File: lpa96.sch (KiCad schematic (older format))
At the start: 26 parts, among them IC1 ATMEGA328-A, P1 CONN_2, P2 CONN_3X2, SW1 SW_PUSH, U1 SD_CARD, U2 LD1117S33, Y1 RESONATEUR

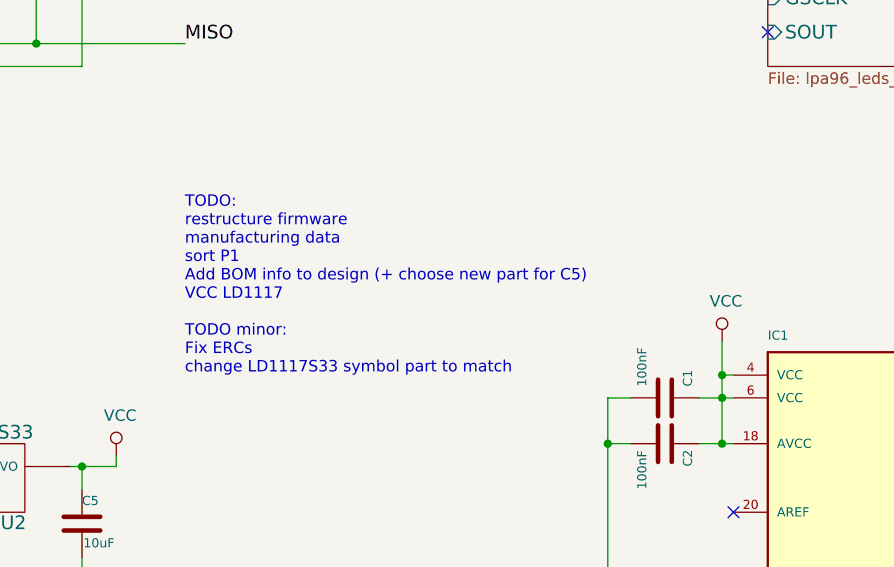
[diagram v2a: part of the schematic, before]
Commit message: done titleblocks, added silkscreen logos
added OSHW and ESD logos to board
filled in titleblocks with title, revision, date, authors
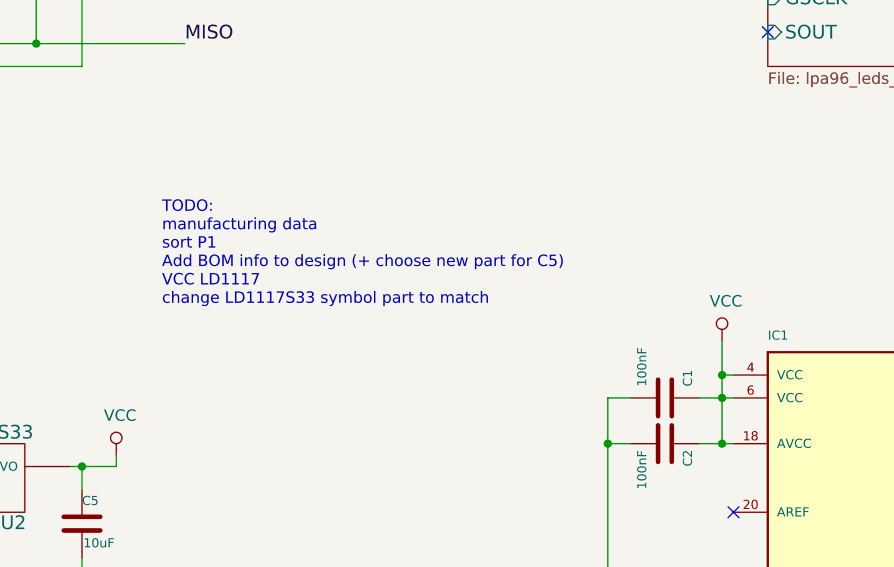
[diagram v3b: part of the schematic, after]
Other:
- note added: "TODO:\nmanufacturing data\nsort P1\nAdd BOM info to design (+ choose new part for C5)\nVCC LD1117\nchange LD1117S33 symbol part to match"
- note removed: "TODO:\nrestructure firmware\nmanufacturing data\nsort P1\nAdd BOM info to design (+ choose new part for C5)\nVCC LD1117\n\nTODO minor:\nFix ERCs\nchange LD1117S33 symbol part to match"
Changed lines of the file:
@@
 encoding utf-8
 Sheet 1 2
-Title ""
-Date "25 jun 2014"
-Rev ""
-Comp ""
+Title "96-well Light Plate Apparatus (LPA), Blue 465nm"
+Date "2019-08-22"
+Rev "2.0"
+Comp "Authors: Tabor lab/Evan Olson/Sebastian Castillo/Open Bioeconomy Lab/Kevin Bibby"
 Comment1 ""
 Comment2 ""
@@
 Text Notes 3650 5800 0    50   ~ 0
 SW1 - Switch to reset processor\nLED97 - lit when running\nLED98 - lit if error\nLED99 - lit once finished\n(LED behaviour software dependant)
-Text Notes 4400 3850 0    50   ~ 0
-TODO:\nrestructure firmware\nmanufacturing data\nsort P1\nAdd BOM info to design (+ choose new part for C5)\nVCC LD1117\n\nTODO minor:\nFix ERCs\nchange LD1117S33 symbol part to match
+Text Notes 4300 3550 0    50   ~ 0
+TODO:\nmanufacturing data\nsort P1\nAdd BOM info to design (+ choose new part for C5)\nVCC LD1117\nchange LD1117S33 symbol part to match
 Wire Wire Line
 	3950 4250 4100 4250

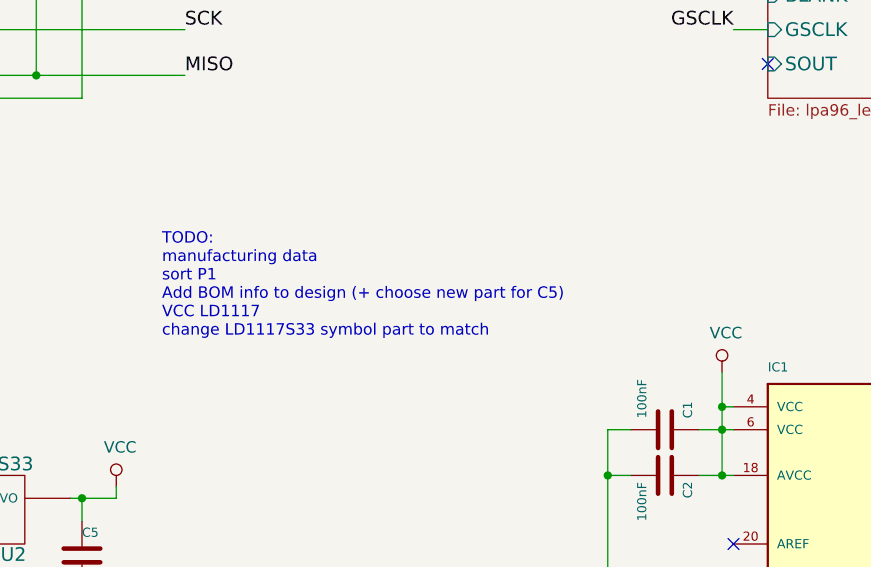
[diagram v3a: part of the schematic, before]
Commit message: title name change, exported final design pack
changed titleblock to remove "blue 465nm" to keep general, removed TODO text ready for export
added full export of design pack (schematic/layout pdfs, step model, gerbers, position & drill files)
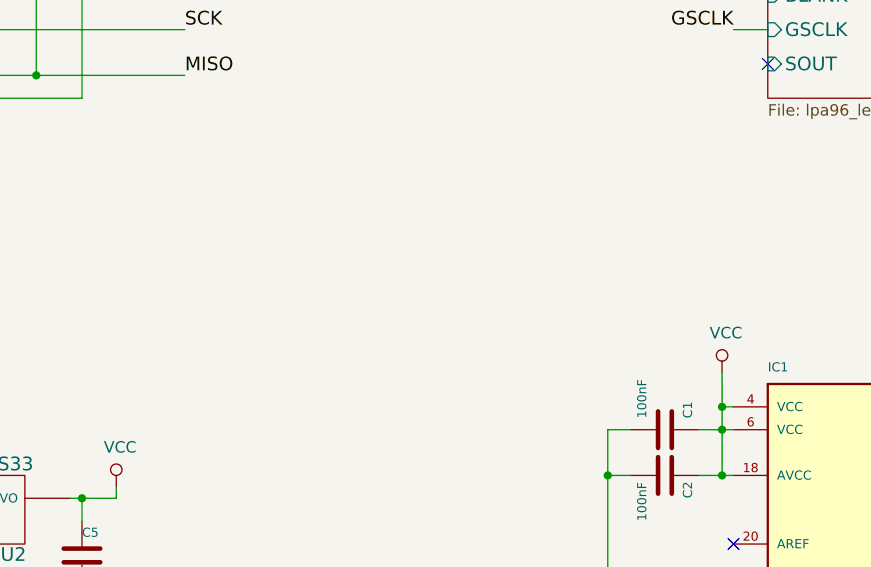
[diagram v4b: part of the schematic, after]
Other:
- note removed: "TODO:\nmanufacturing data\nsort P1\nAdd BOM info to design (+ choose new part for C5)\nVCC LD1117\nchange LD1117S33 symbol part to match"
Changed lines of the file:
@@
 encoding utf-8
 Sheet 1 2
-Title "96-well Light Plate Apparatus (LPA), Blue 465nm"
+Title "96-well Light Plate Apparatus (LPA)"
 Date "2019-08-22"
 Rev "2.0"
@@
 Text Notes 3650 5800 0    50   ~ 0
 SW1 - Switch to reset processor\nLED97 - lit when running\nLED98 - lit if error\nLED99 - lit once finished\n(LED behaviour software dependant)
-Text Notes 4300 3550 0    50   ~ 0
-TODO:\nmanufacturing data\nsort P1\nAdd BOM info to design (+ choose new part for C5)\nVCC LD1117\nchange LD1117S33 symbol part to match
 Wire Wire Line
 	3950 4250 4100 4250

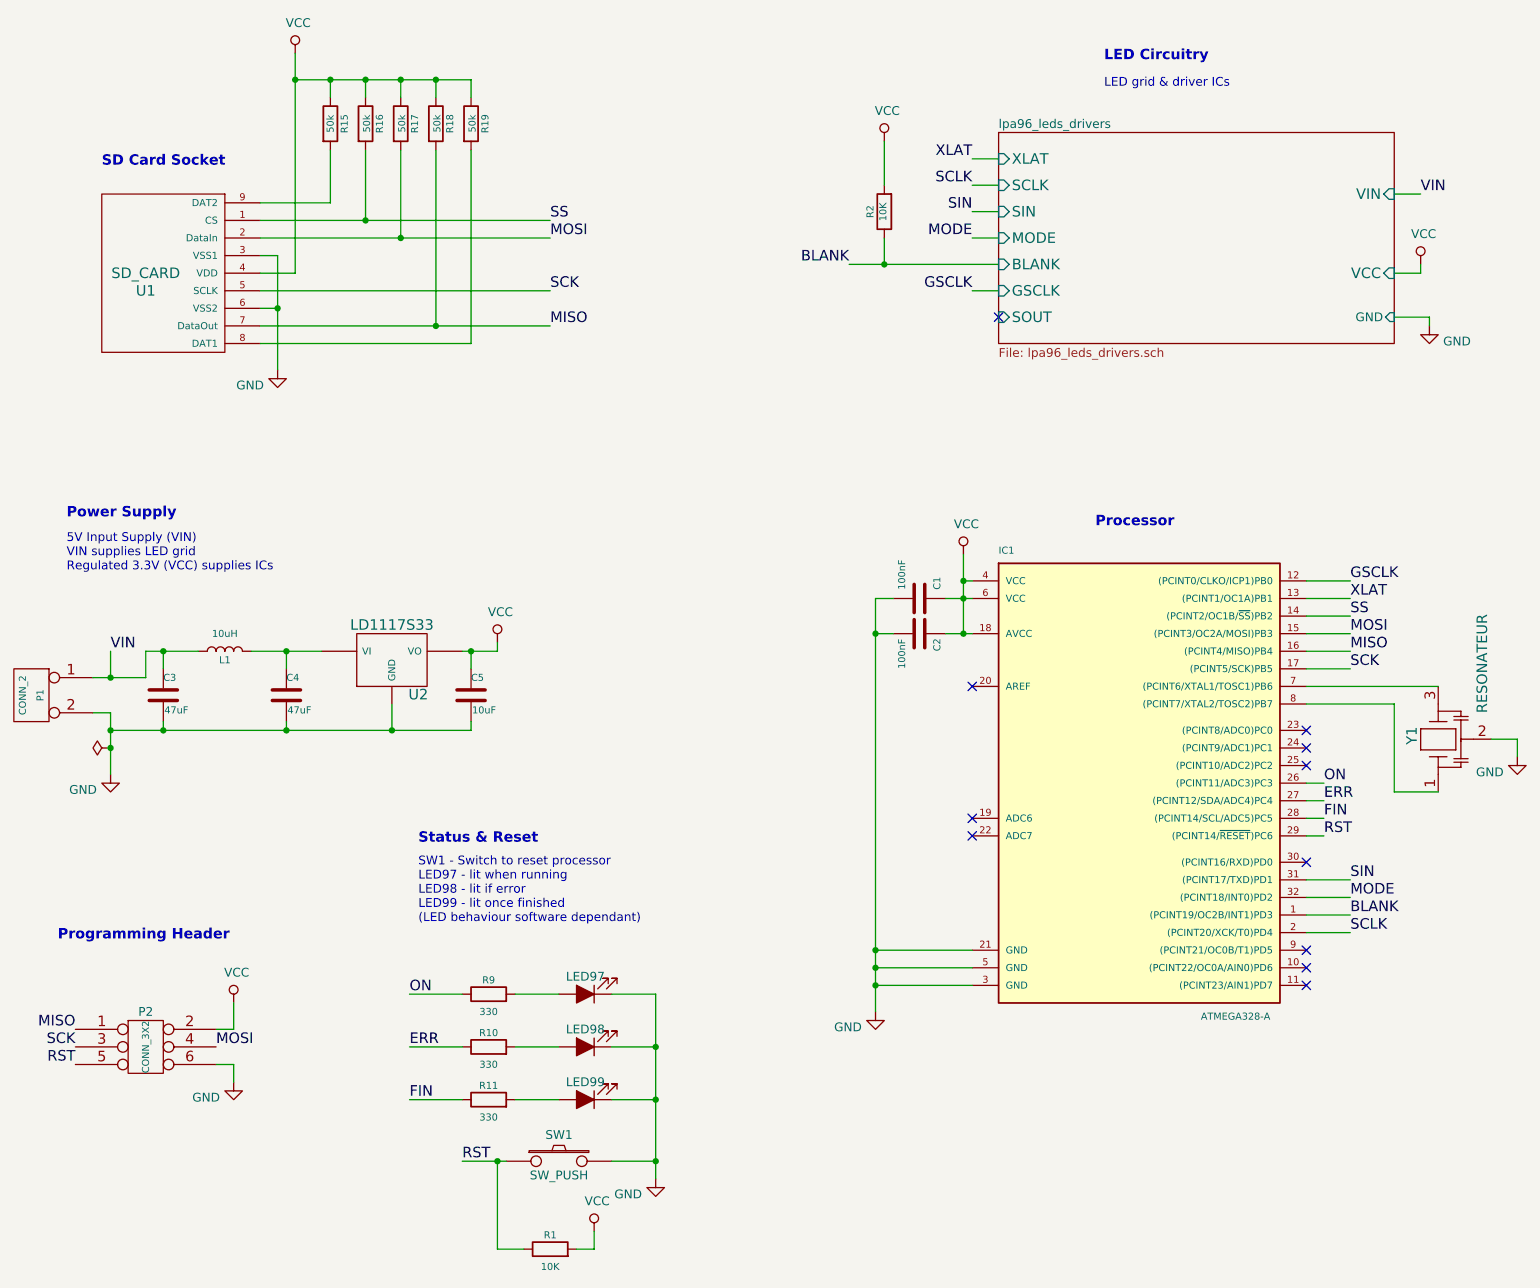
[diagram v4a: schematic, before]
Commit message: small tweaks, added component part numbers & descriptions into design
added all part info from original 24well LPA 'Nature' article (Supplementary Information, Table S1).
part info uses "Description", "Manufacturer1", "MPN1", "Vendor1" and "SKU1" part fields.
changed part info for new LED parts, and C5,C12 chosen part for new case size.
changed P2 to 2x3way exact part rather than 40way breakable header.
changed R15-R19 from 50k to 47k to match part number
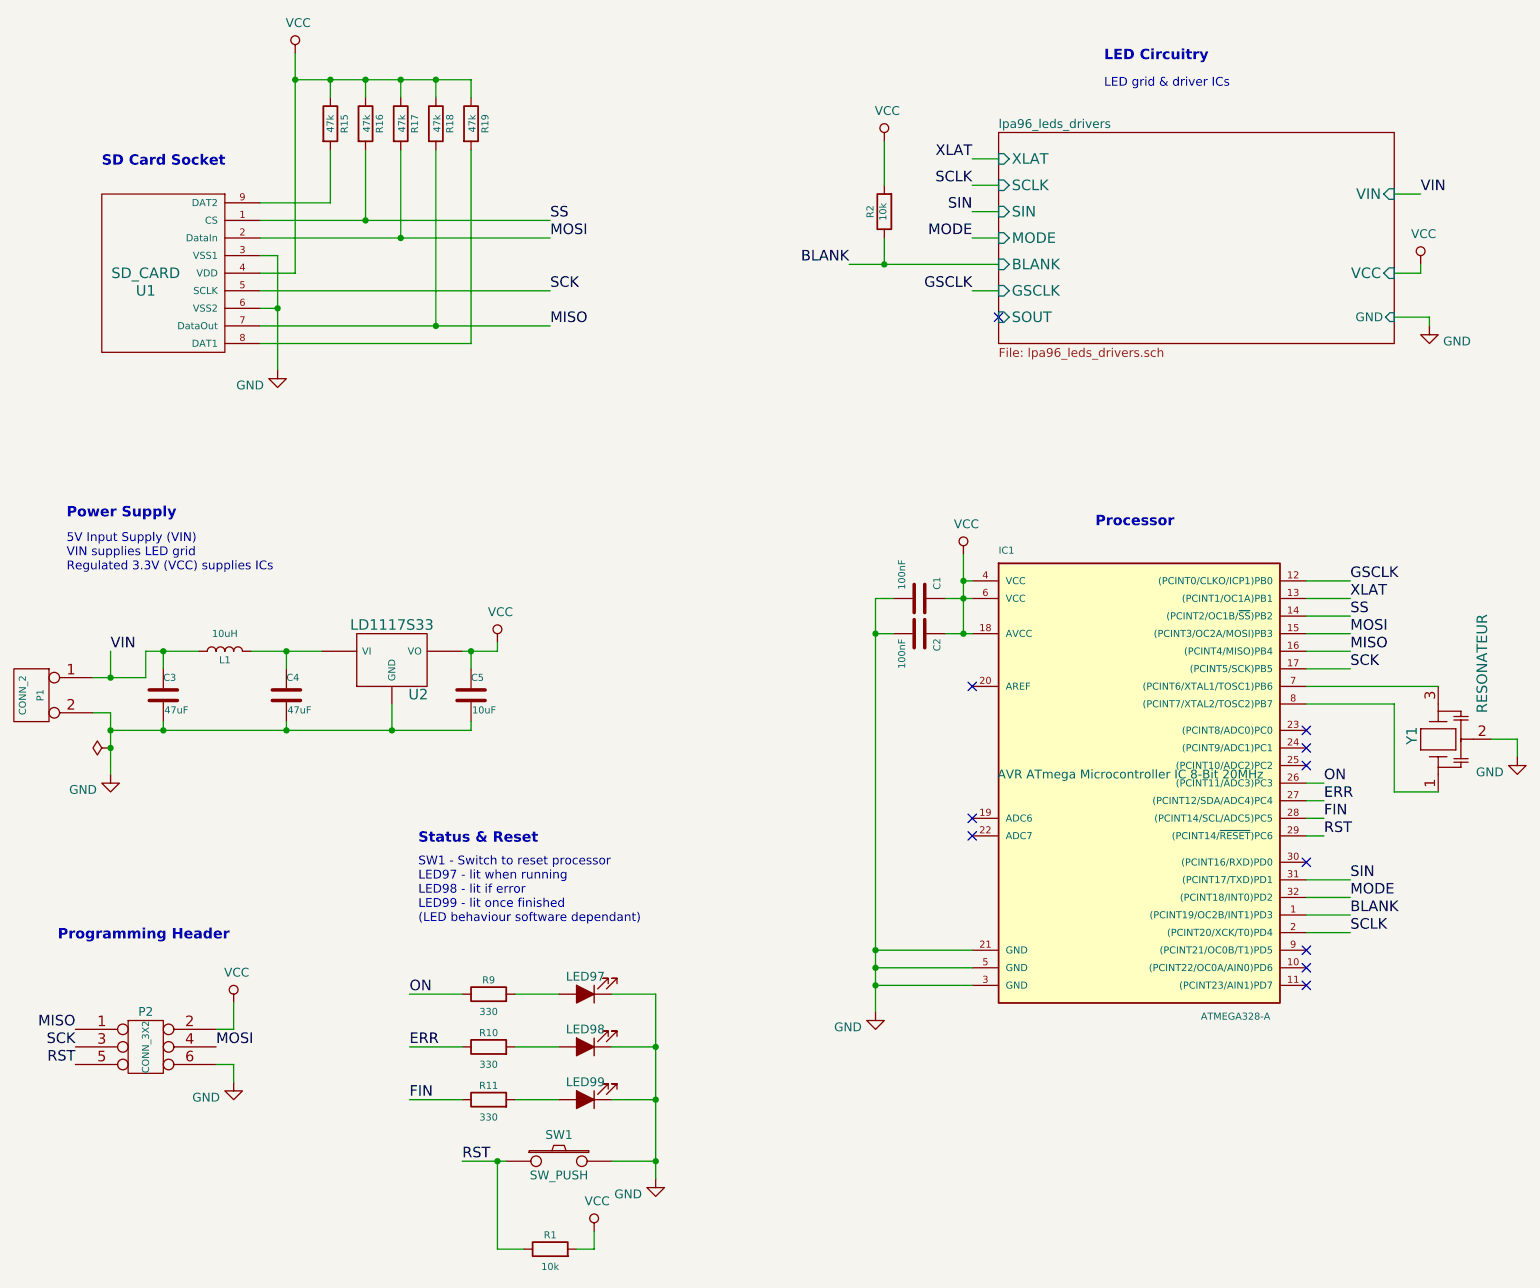
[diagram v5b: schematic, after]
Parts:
- C1, C2: Description (none) -> -20/+80% 50V Y5V SMD MLCC Capacitor 0805; MPN1 (none) -> CL21F104ZBCNNNC; Manufacturer1 (none) -> Samsung; SKU1 (none) -> 1276-1007-1-ND; Vendor1 (none) -> Digikey
- C3, C4: Description (none) -> 20% 35V SMD Electrolytic Capacitor; MPN1 (none) -> UWT1V470MCL1GS; Manufacturer1 (none) -> Nichicon; SKU1 (none) -> 493-2202-1-ND; Vendor1 (none) -> Digikey
- C5: Description (none) -> 10% 25V X5R SMD MLCC Capacitor 1206; MPN1 (none) -> CL31A106KAHNNNE; Manufacturer1 (none) -> Samsung; SKU1 (none) -> 1276-1075-1-ND; Vendor1 (none) -> Digikey
- IC1: Description (none) -> AVR ATmega Microcontroller IC 8-Bit 20MHz; MPN1 (none) -> ATMEGA328-AU; Manufacturer1 (none) -> Microchip; SKU1 (none) -> ATMEGA328-AU-ND; Vendor1 (none) -> Digikey
- L1: Description (none) -> Wirewound Chip Inductor 900mA 1210; MPN1 (none) -> L1210R100MDWIT; Manufacturer1 (none) -> Kemet; SKU1 (none) -> 399-9595-1-ND; Vendor1 (none) -> Digikey
- LED97: Description (none) -> SMD LED Green 0805; MPN1 (none) -> LG R971-KN-1; Manufacturer1 (none) -> OSRAM; SKU1 (none) -> 475-1410-1-ND; Vendor1 (none) -> Digikey
- LED98: Description (none) -> SMD LED Red 0805; MPN1 (none) -> LH R974-LP-1; Manufacturer1 (none) -> OSRAM; SKU1 (none) -> 475-1415-1-ND; Vendor1 (none) -> Digikey
- LED99: Description (none) -> SMD LED Yellow 0805; MPN1 (none) -> LY R976-PS-36; Manufacturer1 (none) -> OSRAM; SKU1 (none) -> 475-2560-1-ND; Vendor1 (none) -> Digikey
- P1: Description (none) -> Connector Male Through Hole 2 position 0.156\" (3.96mm); MPN1 (none) -> 0009652028; Manufacturer1 (none) -> Molex; SKU1 (none) -> WM18823-ND; Vendor1 (none) -> Digikey
- P2: Description (none) -> Header Through Hole 2x3way 6 position 0.1\" (2.54mm); MPN1 (none) -> 67997-206HLF; Manufacturer1 (none) -> Amphenol ICC; SKU1 (none) -> 609-3234-ND; Vendor1 (none) -> Digikey
- R1, R2: value 10K -> 10k; Description (none) -> 5% Chip Resistor 0805; MPN1 (none) -> ERJ-6GEYJ103V; Manufacturer1 (none) -> Panasonic; SKU1 (none) -> P10KACT-ND; Vendor1 (none) -> Digikey
- R10, R11, R9: Description (none) -> 5% Chip Resistor 0805; MPN1 (none) -> RC2012J331CS; Manufacturer1 (none) -> Samsung; SKU1 (none) -> 1276-5519-1-ND; Vendor1 (none) -> Digikey
- R15, R16, R17, R18, R19: value 50k -> 47k; Description (none) -> 5% Chip Resistor 0805; MPN1 (none) -> ERJ-6GEYJ473V; Manufacturer1 (none) -> Panasonic; SKU1 (none) -> P47KACT-ND; Vendor1 (none) -> Digikey
- SW1: Description (none) -> SPST-NO Top Activated SMD Tactile Switch; MPN1 (none) -> PTS645SK43SMTR92 LFS; Manufacturer1 (none) -> C&K; SKU1 (none) -> CKN9084CT-ND; Vendor1 (none) -> Digikey
- U1: Description (none) -> 9 Position Connector SD Card, Surface Mount, Right Angle; MPN1 (none) -> 101-00313-68-02; Manufacturer1 (none) -> Amphenol ICC; SKU1 (none) -> 101-00313-68-02CT-ND; Vendor1 (none) -> Digikey
- U2: Description (none) -> IC Linear Regulator 3.3V 800mA SOT-223; MPN1 (none) -> LD1117S33TR; Manufacturer1 (none) -> ST Microelectronics; SKU1 (none) -> 497-1242-1-ND; Vendor1 (none) -> Digikey
- Y1: Description (none) -> 16MHz Ceramic Resonator SMD; MPN1 (none) -> AWSCR-16.00CV-T; Manufacturer1 (none) -> Abracon; SKU1 (none) -> 535-10008-1-ND; Vendor1 (none) -> Digikey
